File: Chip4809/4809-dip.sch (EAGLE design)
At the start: 20 parts

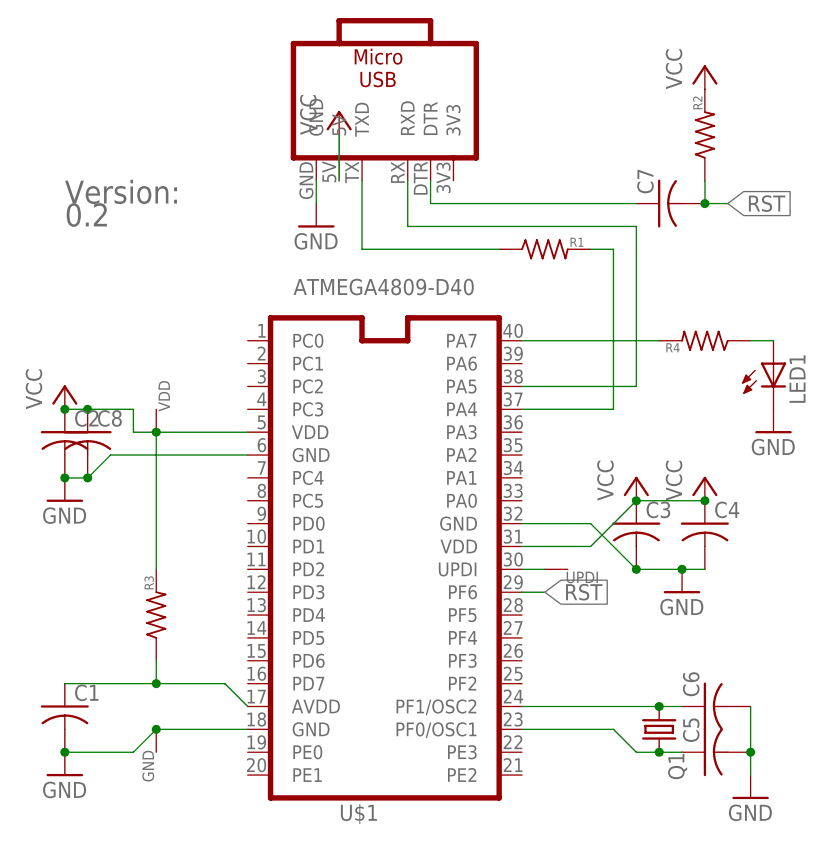
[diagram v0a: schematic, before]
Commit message: Version 0.4 fix RX/TX, move UPDI pin
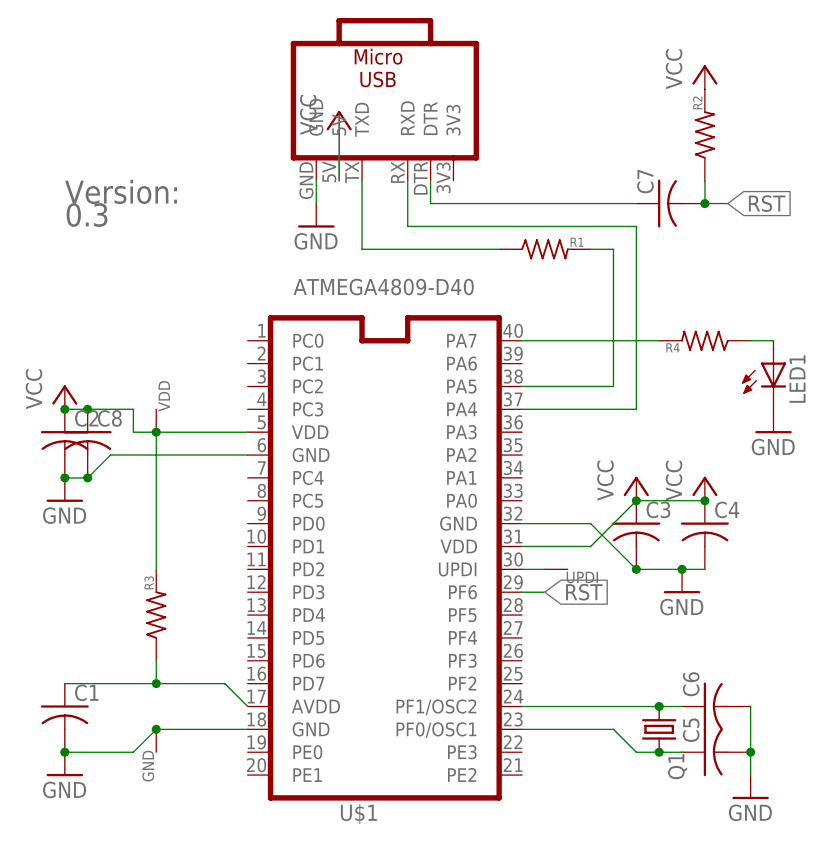
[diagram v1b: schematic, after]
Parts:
- VS1: value 0.2 -> 0.3
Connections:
- net CPURX: now also U$1.PA5; no longer U$1.PA4
- net CPUTX: now also U$1.PA4; no longer U$1.PA5
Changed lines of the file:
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@@
 <grid distance="0.1" unitdist="inch" unit="mm" style="lines" multiple="1" display="no" altdistance="0.01" altunitdist="inch" altunit="inch"/>
 <layers>
-<layer number="1" name="Top" color="4" fill="1" visible="yes" active="no"/>
-<layer number="2" name="Route2" color="1" fill="3" visible="yes" active="no"/>
-<layer number="3" name="Route3" color="4" fill="3" visible="yes" active="no"/>
-<layer number="14" name="Route14" color="1" fill="6" visible="yes" active="no"/>
-<layer number="15" name="Route15" color="4" fill="6" visible="yes" active="no"/>
-<layer number="16" name="Bottom" color="1" fill="1" visible="yes" active="no"/>
-<layer number="17" name="Pads" color="2" fill="1" visible="yes" active="no"/>
-<layer number="18" name="Vias" color="2" fill="1" visible="yes" active="no"/>
-<layer number="19" name="Unrouted" color="6" fill="1" visible="yes" active="no"/>
-<layer number="20" name="Dimension" color="15" fill="1" visible="yes" active="no"/>
-<layer number="21" name="tPlace" color="7" fill="1" visible="yes" active="no"/>
-<layer number="22" name="bPlace" color="7" fill="1" visible="yes" active="no"/>
-<layer number="23" name="tOrigins" color="15" fill="1" visible="yes" active="no"/>
-<layer number="24" name="bOrigins" color="15" fill="1" visible="yes" active="no"/>
-<layer number="25" name="tNames" color="7" fill="1" visible="yes" active="no"/>
-<layer number="26" name="bNames" color="7" fill="1" visible="yes" active="no"/>
-<layer number="27" name="tValues" color="7" fill="1" visible="yes" active="no"/>
-<layer number="28" name="bValues" color="7" fill="1" visible="yes" active="no"/>
+<layer number="1" name="Top" color="4" fill="1" visible="no" active="no"/>
+<layer number="2" name="Route2" color="1" fill="3" visible="no" active="no"/>
+<layer number="3" name="Route3" color="4" fill="3" visible="no" active="no"/>
+<layer number="14" name="Route14" color="1" fill="6" visible="no" active="no"/>
+<layer number="15" name="Route15" color="4" fill="6" visible="no" active="no"/>
+<layer number="16" name="Bottom" color="1" fill="1" visible="no" active="no"/>
+<layer number="17" name="Pads" color="2" fill="1" visible="no" active="no"/>
+<layer number="18" name="Vias" color="2" fill="1" visible="no" active="no"/>
+<layer number="19" name="Unrouted" color="6" fill="1" visible="no" active="no"/>
+<layer number="20" name="Dimension" color="15" fill="1" visible="no" active="no"/>
+<layer number="21" name="tPlace" color="7" fill="1" visible="no" active="no"/>
+<layer number="22" name="bPlace" color="7" fill="1" visible="no" active="no"/>
+<layer number="23" name="tOrigins" color="15" fill="1" visible="no" active="no"/>
+<layer number="24" name="bOrigins" color="15" fill="1" visible="no" active="no"/>
+<layer number="25" name="tNames" color="7" fill="1" visible="no" active="no"/>
+<layer number="26" name="bNames" color="7" fill="1" visible="no" active="no"/>
+<layer number="27" name="tValues" color="7" fill="1" visible="no" active="no"/>
+<layer number="28" name="bValues" color="7" fill="1" visible="no" active="no"/>
 <layer number="29" name="tStop" color="7" fill="3" visible="no" active="no"/>
 <layer number="30" name="bStop" color="7" fill="6" visible="no" active="no"/>
@@
 <layer number="35" name="tGlue" color="7" fill="4" visible="no" active="no"/>
 <layer number="36" name="bGlue" color="7" fill="5" visible="no" active="no"/>
-<layer number="37" name="tTest" color="7" fill="1" visible="yes" active="no"/>
-<layer number="38" name="bTest" color="7" fill="1" visible="yes" active="no"/>
+<layer number="37" name="tTest" color="7" fill="1" visible="no" active="no"/>
+<layer number="38" name="bTest" color="7" fill="1" visible="no" active="no"/>
 <layer number="39" name="tKeepout" color="4" fill="11" visible="no" active="no"/>
 <layer number="40" name="bKeepout" color="1" fill="11" visible="no" active="no"/>
@@
 <layer number="44" name="Drills" color="7" fill="1" visible="no" active="no"/>
 <layer number="45" name="Holes" color="7" fill="1" visible="no" active="no"/>
-<layer number="46" name="Milling" color="3" fill="1" visible="yes" active="no"/>
-<layer number="47" name="Measures" color="7" fill="1" visible="yes" active="no"/>
-<layer number="48" name="Document" color="7" fill="1" visible="yes" active="no"/>
-<layer number="49" name="Reference" color="7" fill="1" visible="yes" active="no"/>
-<layer number="50" name="dxf" color="7" fill="1" visible="yes" active="no"/>
-<layer number="51" name="tDocu" color="7" fill="1" visible="yes" active="no"/>
-<layer number="52" name="bDocu" color="7" fill="1" visible="yes" active="no"/>
-<layer number="53" name="tGND_GNDA" color="7" fill="9" visible="yes" active="no"/>
-<layer number="54" name="bGND_GNDA" color="1" fill="9" visible="yes" active="no"/>
-<layer number="56" name="wert" color="7" fill="1" visible="yes" active="no"/>
-<layer number="57" name="tCAD" color="7" fill="1" visible="yes" active="no"/>
+<layer number="46" name="Milling" color="3" fill="1" visible="no" active="no"/>
+<layer number="47" name="Measures" color="7" fill="1" visible="no" active="no"/>
+<layer number="48" name="Document" color="7" fill="1" visible="no" active="no"/>
+<layer number="49" name="Reference" color="7" fill="1" visible="no" active="no"/>
+<layer number="50" name="dxf" color="7" fill="1" visible="no" active="no"/>
+<layer number="51" name="tDocu" color="7" fill="1" visible="no" active="no"/>
+<layer number="52" name="bDocu" color="7" fill="1" visible="no" active="no"/>
+<layer number="53" name="tGND_GNDA" color="7" fill="9" visible="no" active="no"/>
+<layer number="54" name="bGND_GNDA" color="1" fill="9" visible="no" active="no"/>
+<layer number="56" name="wert" color="7" fill="1" visible="no" active="no"/>
+<layer number="57" name="tCAD" color="7" fill="1" visible="no" active="no"/>
 <layer number="90" name="Modules" color="5" fill="1" visible="yes" active="yes"/>
 <layer number="91" name="Nets" color="2" fill="1" visible="yes" active="yes"/>
@@
 <part name="R3" library="my-rcl" deviceset="R-US_" device="R0805"/>
 <part name="C8" library="my-rcl" deviceset="C-US" device="C1206"/>
-<part name="VS1" library="mylib4" deviceset="VERSIONSTRING" device="" value="0.2"/>
+<part name="VS1" library="mylib4" deviceset="VERSIONSTRING" device="" value="0.3"/>
 <part name="R4" library="my-rcl" deviceset="R-US_" device="R0805"/>
 <part name="LED1" library="my-led" deviceset="LED" device="CHIP-LED0805"/>
@@
 <net name="CPUTX" class="0">
 <segment>
-<pinref part="U$1" gate="G$1" pin="PA5"/>
-<wire x1="76.2" y1="63.5" x2="88.9" y2="63.5" width="0.1524" layer="91"/>
-<wire x1="88.9" y1="63.5" x2="88.9" y2="81.28" width="0.1524" layer="91"/>
+<wire x1="88.9" y1="60.96" x2="88.9" y2="81.28" width="0.1524" layer="91"/>
 <pinref part="MOD1" gate="G$1" pin="RXD"/>
 <wire x1="63.5" y1="86.36" x2="63.5" y2="81.28" width="0.1524" layer="91"/>
 <wire x1="88.9" y1="81.28" x2="63.5" y2="81.28" width="0.1524" layer="91"/>
+<pinref part="U$1" gate="G$1" pin="PA4"/>
+<wire x1="76.2" y1="60.96" x2="88.9" y2="60.96" width="0.1524" layer="91"/>
 </segment>
 </net>
 <net name="CPURX" class="0">
 <segment>
-<pinref part="U$1" gate="G$1" pin="PA4"/>
-<wire x1="76.2" y1="60.96" x2="86.36" y2="60.96" width="0.1524" layer="91"/>
-<wire x1="86.36" y1="60.96" x2="86.36" y2="78.74" width="0.1524" layer="91"/>
 <pinref part="R1" gate="G$1" pin="2"/>
+<wire x1="86.36" y1="63.5" x2="86.36" y2="78.74" width="0.1524" layer="91"/>
 <wire x1="86.36" y1="78.74" x2="83.82" y2="78.74" width="0.1524" layer="91"/>
-</segment>
-</net>
+<pinref part="U$1" gate="G$1" pin="PA5"/>
+<wire x1="76.2" y1="63.5" x2="86.36" y2="63.5" width="0.1524" layer="91"/>
+</segment>
+</net>
